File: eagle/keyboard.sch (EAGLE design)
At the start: 72 parts, among them Q1 12MHz

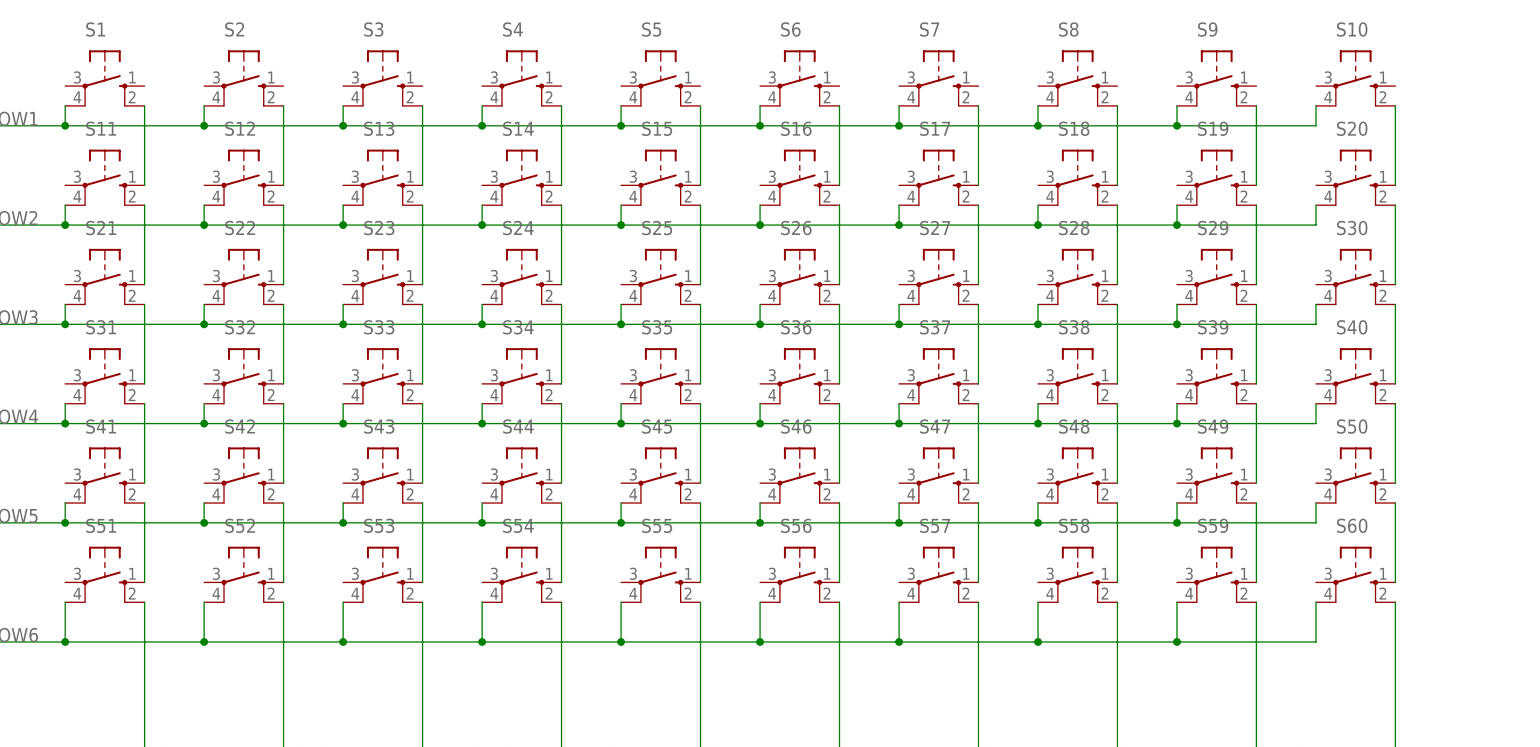
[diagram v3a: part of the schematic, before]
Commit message: Fix schematic button matrix
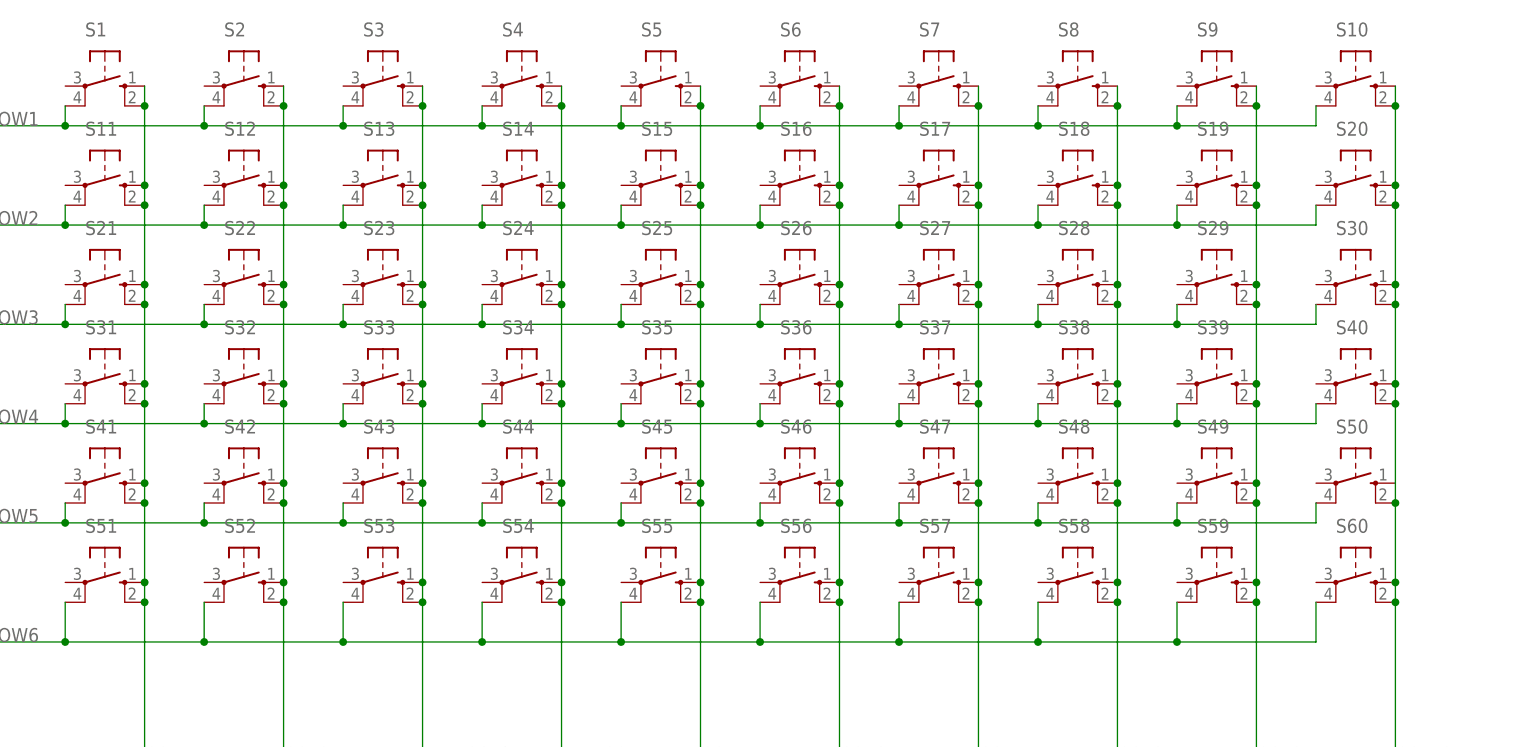
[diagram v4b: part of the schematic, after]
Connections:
- removed net N$1: S1.S1, S11.S
- removed net N$10: S42.S1, S52.S
- removed net N$11: S13.S, S3.S1
- removed net N$12: S13.S1, S23.S
- removed net N$13: S23.S1, S33.S
- removed net N$14: S33.S1, S43.S
- removed net N$15: S43.S1, S53.S
- removed net N$16: S14.S, S4.S1
- removed net N$17: S14.S1, S24.S
- removed net N$18: S24.S1, S34.S
- removed net N$19: S34.S1, S44.S
- removed net N$2: S11.S1, S21.S
- removed net N$20: S44.S1, S54.S
- removed net N$21: S15.S, S5.S1
- removed net N$22: S15.S1, S25.S
- removed net N$23: S25.S1, S35.S
- removed net N$24: S35.S1, S45.S
- removed net N$25: S45.S1, S55.S
- removed net N$26: S16.S, S6.S1
- removed net N$27: S16.S1, S26.S
- removed net N$28: S26.S1, S36.S
- removed net N$29: S36.S1, S46.S
- removed net N$3: S21.S1, S31.S
- removed net N$30: S46.S1, S56.S
- removed net N$31: S17.S, S7.S1
- removed net N$32: S17.S1, S27.S
- removed net N$33: S27.S1, S37.S
- removed net N$34: S37.S1, S47.S
- removed net N$35: S47.S1, S57.S
- removed net N$36: S18.S, S8.S1
- removed net N$37: S18.S1, S28.S
- removed net N$38: S28.S1, S38.S
- removed net N$39: S38.S1, S48.S
- removed net N$4: S31.S1, S41.S
- removed net N$40: S48.S1, S58.S
- removed net N$41: S49.S1, S59.S
- removed net N$42: S29.S1, S39.S
- removed net N$43: S19.S1, S29.S
- removed net N$44: S19.S, S9.S1
- removed net N$45: S10.S1, S20.S
- removed net N$46: S20.S1, S30.S
- removed net N$47: S30.S1, S40.S
- removed net N$48: S40.S1, S50.S
- removed net N$49: S39.S1, S49.S
- removed net N$5: S41.S1, S51.S
- removed net N$50: S50.S1, S60.S
- removed net N$6: S12.S, S2.S1
- removed net N$7: S12.S1, S22.S
- removed net N$8: S22.S1, S32.S
- removed net N$9: S32.S1, S42.S
- net COL1: now also S1.S, S1.S1, S11.S, S11.S1, S21.S, S21.S1, S31.S, S31.S1, S41.S, S41.S1, S51.S
- net COL10: now also S10.S, S10.S1, S20.S, S20.S1, S30.S, S30.S1, S40.S, S40.S1, S50.S, S50.S1, S60.S
- net COL2: now also S12.S, S12.S1, S2.S, S2.S1, S22.S, S22.S1, S32.S, S32.S1, S42.S, S42.S1, S52.S
- net COL5: now also S15.S, S15.S1, S25.S, S25.S1, S35.S, S35.S1, S45.S, S45.S1, S5.S, S5.S1, S55.S
- net COL6: now also S16.S, S16.S1, S26.S, S26.S1, S36.S, S36.S1, S46.S, S46.S1, S56.S, S6.S, S6.S1
- net COL7: now also S17.S, S17.S1, S27.S, S27.S1, S37.S, S37.S1, S47.S, S47.S1, S57.S, S7.S, S7.S1
- net COL8: now also S18.S, S18.S1, S28.S, S28.S1, S38.S, S38.S1, S48.S, S48.S1, S58.S, S8.S, S8.S1
- net COL9: now also S19.S, S19.S1, S29.S, S29.S1, S39.S, S39.S1, S49.S, S49.S1, S59.S, S9.S, S9.S1
- net RXD/COL3: now also S13.S, S13.S1, S23.S, S23.S1, S3.S, S3.S1, S33.S, S33.S1, S43.S, S43.S1, S53.S
- net TXD/COL4: now also S14.S, S14.S1, S24.S, S24.S1, S34.S, S34.S1, S4.S, S4.S1, S44.S, S44.S1, S54.S

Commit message: Finish basic board design
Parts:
- IC1: value STC12C5616AD-28PIN -> STC12C5616AD
- renumbered U$1 to IC1
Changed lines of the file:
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@@
 <part name="S59" library="switch-omron" library_urn="urn:adsk.eagle:library:377" deviceset="10-XX" device="" package3d_urn="urn:adsk.eagle:package:27496/1"/>
 <part name="S60" library="switch-omron" library_urn="urn:adsk.eagle:library:377" deviceset="10-XX" device="" package3d_urn="urn:adsk.eagle:package:27496/1"/>
-<part name="U$1" library="TCalc" deviceset="STC12C5616AD-28PIN" device="" package3d_urn="urn:adsk.eagle:package:6673337/1"/>
+<part name="IC1" library="TCalc" deviceset="STC12C5616AD-28PIN" device="" package3d_urn="urn:adsk.eagle:package:6673337/1" value="STC12C5616AD"/>
 <part name="J3" library="pinhead" library_urn="urn:adsk.eagle:library:325" deviceset="PINHD-1X5" device="" package3d_urn="urn:adsk.eagle:package:22469/2"/>
 <part name="GND1" library="supply1" library_urn="urn:adsk.eagle:library:371" deviceset="GND" device=""/>
@@
 <attribute name="VALUE" x="234.315" y="135.89" size="1.778" layer="96"/>
 </instance>
-<instance part="U$1" gate="G$1" x="109.22" y="58.42" smashed="yes"/>
+<instance part="IC1" gate="G$1" x="109.22" y="58.42" smashed="yes"/>
 <instance part="J3" gate="A" x="182.88" y="73.66" smashed="yes">
 <attribute name="NAME" x="176.53" y="81.915" size="1.778" layer="95"/>
@@
 </segment>
 <segment>
-<pinref part="U$1" gate="G$1" pin="P1.7"/>
+<pinref part="IC1" gate="G$1" pin="P1.7"/>
 <wire x1="124.46" y1="71.12" x2="132.08" y2="71.12" width="0.1524" layer="91"/>
 <label x="124.46" y="71.12" size="1.778" layer="95"/>
@@
 </segment>
 <segment>
-<pinref part="U$1" gate="G$1" pin="P2.0"/>
+<pinref part="IC1" gate="G$1" pin="P2.0"/>
 <wire x1="124.46" y1="73.66" x2="132.08" y2="73.66" width="0.1524" layer="91"/>
 <label x="124.46" y="73.66" size="1.778" layer="95"/>
@@
 <net name="ROW3" class="0">
 <segment>
-<pinref part="U$1" gate="G$1" pin="P2.1"/>
+<pinref part="IC1" gate="G$1" pin="P2.1"/>
 <wire x1="124.46" y1="76.2" x2="132.08" y2="76.2" width="0.1524" layer="91"/>
 <label x="124.46" y="76.2" size="1.778" layer="95"/>
@@
 <net name="GND" class="0">
 <segment>
-<pinref part="U$1" gate="G$1" pin="GND"/>
+<pinref part="IC1" gate="G$1" pin="GND"/>
 <pinref part="GND1" gate="1" pin="GND"/>
 <wire x1="93.98" y1="45.72" x2="93.98" y2="25.4" width="0.1524" layer="91"/>
@@
 <label x="170.18" y="73.66" size="1.778" layer="95"/>
 <wire x1="162.56" y1="73.66" x2="162.56" y2="55.88" width="0.1524" layer="91"/>
-<pinref part="U$1" gate="G$1" pin="P1.1"/>
+<pinref part="IC1" gate="G$1" pin="P1.1"/>
 <wire x1="162.56" y1="55.88" x2="124.46" y2="55.88" width="0.1524" layer="91"/>
 <label x="124.46" y="55.88" size="1.778" layer="95"/>
@@
 <wire x1="180.34" y1="71.12" x2="165.1" y2="71.12" width="0.1524" layer="91"/>
 <label x="170.18" y="71.12" size="1.778" layer="95"/>
-<pinref part="U$1" gate="G$1" pin="P1.2"/>
+<pinref part="IC1" gate="G$1" pin="P1.2"/>
 <wire x1="165.1" y1="71.12" x2="165.1" y2="58.42" width="0.1524" layer="91"/>
 <wire x1="165.1" y1="58.42" x2="124.46" y2="58.42" width="0.1524" layer="91"/>
@@
 <wire x1="167.64" y1="68.58" x2="167.64" y2="53.34" width="0.1524" layer="91"/>
 <label x="170.18" y="68.58" size="1.778" layer="95"/>
-<pinref part="U$1" gate="G$1" pin="P1.0"/>
+<pinref part="IC1" gate="G$1" pin="P1.0"/>
 <wire x1="124.46" y1="53.34" x2="167.64" y2="53.34" width="0.1524" layer="91"/>
 <label x="124.46" y="53.34" size="1.778" layer="95"/>
@@
 <segment>
 <label x="182.88" y="43.18" size="1.778" layer="95"/>
-<pinref part="U$1" gate="G$1" pin="P1.6"/>
+<pinref part="IC1" gate="G$1" pin="P1.6"/>
 <wire x1="154.94" y1="43.18" x2="170.18" y2="43.18" width="0.1524" layer="91"/>
 <wire x1="170.18" y1="43.18" x2="198.12" y2="43.18" width="0.1524" layer="91"/>
@@
 <label x="182.88" y="40.64" size="1.778" layer="95"/>
 <wire x1="152.4" y1="40.64" x2="152.4" y2="66.04" width="0.1524" layer="91"/>
-<pinref part="U$1" gate="G$1" pin="P1.5"/>
+<pinref part="IC1" gate="G$1" pin="P1.5"/>
 <wire x1="152.4" y1="66.04" x2="124.46" y2="66.04" width="0.1524" layer="91"/>
 <label x="124.46" y="66.04" size="1.778" layer="95"/>
@@
 <wire x1="149.86" y1="38.1" x2="180.34" y2="38.1" width="0.1524" layer="91"/>
 <label x="182.88" y="38.1" size="1.778" layer="95"/>
-<pinref part="U$1" gate="G$1" pin="P1.4"/>
+<pinref part="IC1" gate="G$1" pin="P1.4"/>
 <wire x1="180.34" y1="38.1" x2="198.12" y2="38.1" width="0.1524" layer="91"/>
 <wire x1="124.46" y1="63.5" x2="149.86" y2="63.5" width="0.1524" layer="91"/>
@@
 <net name="XTAL2" class="0">
 <segment>
-<pinref part="U$1" gate="G$1" pin="XTAL2"/>
+<pinref part="IC1" gate="G$1" pin="XTAL2"/>
 <wire x1="93.98" y1="66.04" x2="81.28" y2="66.04" width="0.1524" layer="91"/>
 <label x="86.36" y="66.04" size="1.778" layer="95"/>
@@
 <net name="XTAL1" class="0">
 <segment>
-<pinref part="U$1" gate="G$1" pin="XTAL1"/>
+<pinref part="IC1" gate="G$1" pin="XTAL1"/>
 <label x="86.36" y="63.5" size="1.778" layer="95"/>
 <wire x1="83.82" y1="63.5" x2="93.98" y2="63.5" width="0.1524" layer="91"/>
@@
 <net name="COL1" class="0">
 <segment>
-<pinref part="U$1" gate="G$1" pin="P2.2"/>
+<pinref part="IC1" gate="G$1" pin="P2.2"/>
 <wire x1="93.98" y1="78.74" x2="86.36" y2="78.74" width="0.1524" layer="91"/>
 <label x="86.36" y="78.74" size="1.778" layer="95"/>
@@
 <net name="COL2" class="0">
 <segment>
-<pinref part="U$1" gate="G$1" pin="P2.3"/>
+<pinref part="IC1" gate="G$1" pin="P2.3"/>
 <wire x1="93.98" y1="76.2" x2="86.36" y2="76.2" width="0.1524" layer="91"/>
 <label x="86.36" y="76.2" size="1.778" layer="95"/>
@@
 <net name="COL5" class="0">
 <segment>
-<pinref part="U$1" gate="G$1" pin="P3.2"/>
+<pinref part="IC1" gate="G$1" pin="P3.2"/>
 <wire x1="93.98" y1="60.96" x2="86.36" y2="60.96" width="0.1524" layer="91"/>
 <label x="86.36" y="60.96" size="1.778" layer="95"/>
@@
 <net name="COL6" class="0">
 <segment>
-<pinref part="U$1" gate="G$1" pin="P3.3"/>
+<pinref part="IC1" gate="G$1" pin="P3.3"/>
 <wire x1="93.98" y1="58.42" x2="86.36" y2="58.42" width="0.1524" layer="91"/>
 <label x="86.36" y="58.42" size="1.778" layer="95"/>
@@
 <net name="COL7" class="0">
 <segment>
-<pinref part="U$1" gate="G$1" pin="P3.4"/>
+<pinref part="IC1" gate="G$1" pin="P3.4"/>
 <wire x1="93.98" y1="55.88" x2="86.36" y2="55.88" width="0.1524" layer="91"/>
 <label x="86.36" y="55.88" size="1.778" layer="95"/>
@@
 <net name="COL8" class="0">
 <segment>
-<pinref part="U$1" gate="G$1" pin="P3.5"/>
+<pinref part="IC1" gate="G$1" pin="P3.5"/>
 <wire x1="93.98" y1="53.34" x2="86.36" y2="53.34" width="0.1524" layer="91"/>
 <label x="86.36" y="53.34" size="1.778" layer="95"/>
@@
 <net name="COL9" class="0">
 <segment>
-<pinref part="U$1" gate="G$1" pin="P2.4"/>
+<pinref part="IC1" gate="G$1" pin="P2.4"/>
 <wire x1="93.98" y1="50.8" x2="86.36" y2="50.8" width="0.1524" layer="91"/>
 <label x="86.36" y="50.8" size="1.778" layer="95"/>
@@
 <net name="COL10" class="0">
 <segment>
-<pinref part="U$1" gate="G$1" pin="P2.5"/>
+<pinref part="IC1" gate="G$1" pin="P2.5"/>
 <wire x1="93.98" y1="48.26" x2="86.36" y2="48.26" width="0.1524" layer="91"/>
 <label x="86.36" y="48.26" size="1.778" layer="95"/>
@@
 <net name="VCC" class="0">
 <segment>
-<pinref part="U$1" gate="G$1" pin="VCC"/>
+<pinref part="IC1" gate="G$1" pin="VCC"/>
 <label x="124.46" y="78.74" size="1.778" layer="95"/>
 <pinref part="P+1" gate="VCC" pin="VCC"/>
@@
 <net name="RXD/COL3" class="0">
 <segment>
-<pinref part="U$1" gate="G$1" pin="RXD/P3.0"/>
+<pinref part="IC1" gate="G$1" pin="RXD/P3.0"/>
 <wire x1="63.5" y1="71.12" x2="93.98" y2="71.12" width="0.1524" layer="91"/>
 <label x="81.28" y="71.12" size="1.778" layer="95"/>
@@
 <net name="TXD/COL4" class="0">
 <segment>
-<pinref part="U$1" gate="G$1" pin="TXD/P3.1"/>
+<pinref part="IC1" gate="G$1" pin="TXD/P3.1"/>
 <wire x1="63.5" y1="68.58" x2="93.98" y2="68.58" width="0.1524" layer="91"/>
 <label x="81.28" y="68.58" size="1.778" layer="95"/>
@@
 </segment>
 <segment>
-<pinref part="U$1" gate="G$1" pin="P2.6"/>
+<pinref part="IC1" gate="G$1" pin="P2.6"/>
 <wire x1="124.46" y1="45.72" x2="132.08" y2="45.72" width="0.1524" layer="91"/>
 <label x="124.46" y="45.72" size="1.778" layer="95"/>
@@
 </segment>
 <segment>
-<pinref part="U$1" gate="G$1" pin="P2.7"/>
+<pinref part="IC1" gate="G$1" pin="P2.7"/>
 <wire x1="124.46" y1="48.26" x2="132.08" y2="48.26" width="0.1524" layer="91"/>
 <label x="124.46" y="48.26" size="1.778" layer="95"/>
@@
 </segment>
 <segment>
-<pinref part="U$1" gate="G$1" pin="P3.7"/>
+<pinref part="IC1" gate="G$1" pin="P3.7"/>
 <wire x1="124.46" y1="50.8" x2="132.08" y2="50.8" width="0.1524" layer="91"/>
 <label x="124.46" y="50.8" size="1.778" layer="95"/>

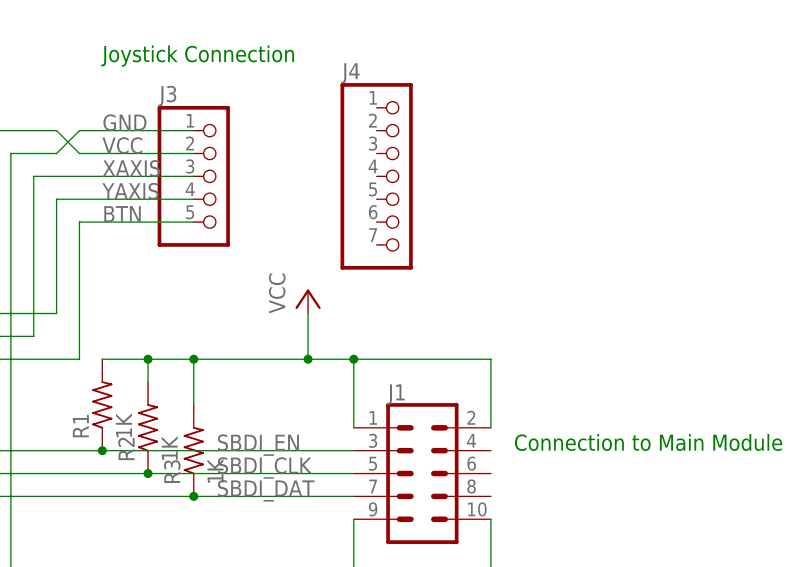
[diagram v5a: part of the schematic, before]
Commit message: Finish keyboard PCB
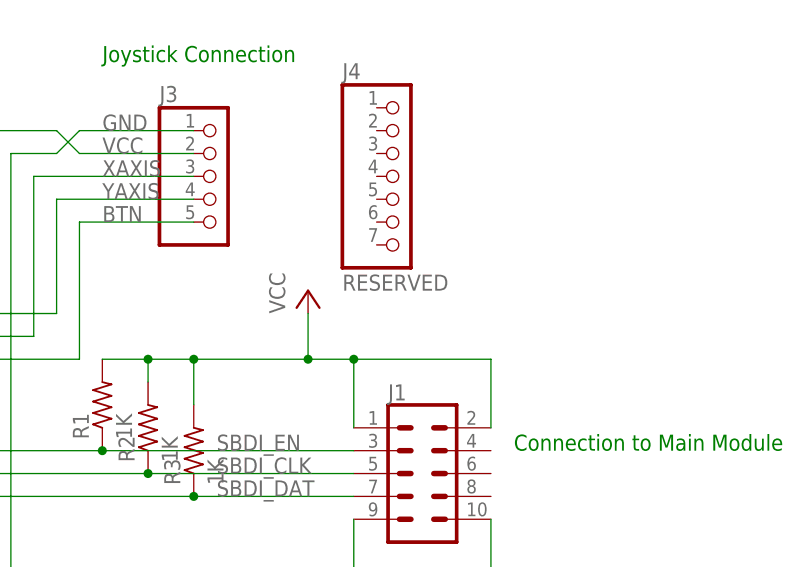
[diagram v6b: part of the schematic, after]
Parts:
- J4: value (none) -> RESERVED
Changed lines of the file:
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@@
 <part name="J1" library="SparkFun-Connectors" library_urn="urn:adsk.eagle:library:513" deviceset="CONN_05X2" device="SHD_LOCK" package3d_urn="urn:adsk.eagle:package:38007/1"/>
 <part name="C3" library="rcl" library_urn="urn:adsk.eagle:library:334" deviceset="C-EU" device="025-030X050" package3d_urn="urn:adsk.eagle:package:23631/1" value="0.1uF"/>
-<part name="J4" library="pinhead" library_urn="urn:adsk.eagle:library:325" deviceset="PINHD-1X7" device="" package3d_urn="urn:adsk.eagle:package:22477/2"/>
+<part name="J4" library="pinhead" library_urn="urn:adsk.eagle:library:325" deviceset="PINHD-1X7" device="" package3d_urn="urn:adsk.eagle:package:22477/2" value="RESERVED"/>
 </parts>
 <sheets>
